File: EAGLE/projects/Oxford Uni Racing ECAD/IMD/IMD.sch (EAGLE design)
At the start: 6 parts, among them IC1 LM2901N, J1 T821108A1S100CEU, K1 RT444012, T1 BT169

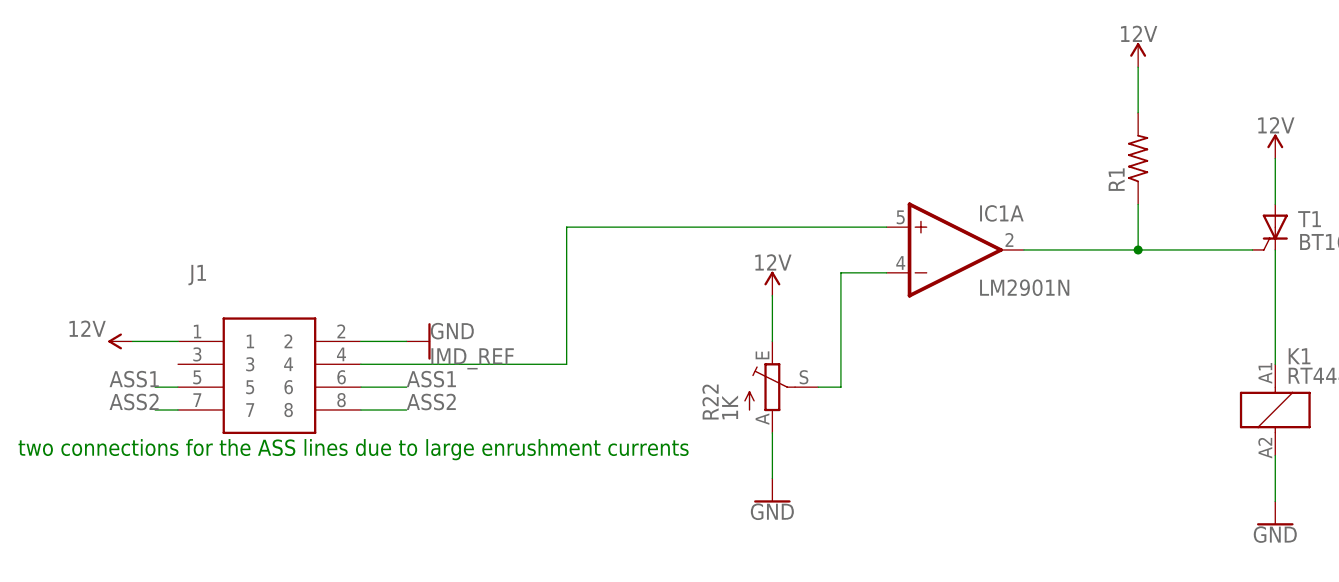
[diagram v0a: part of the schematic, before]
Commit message: routed IMD
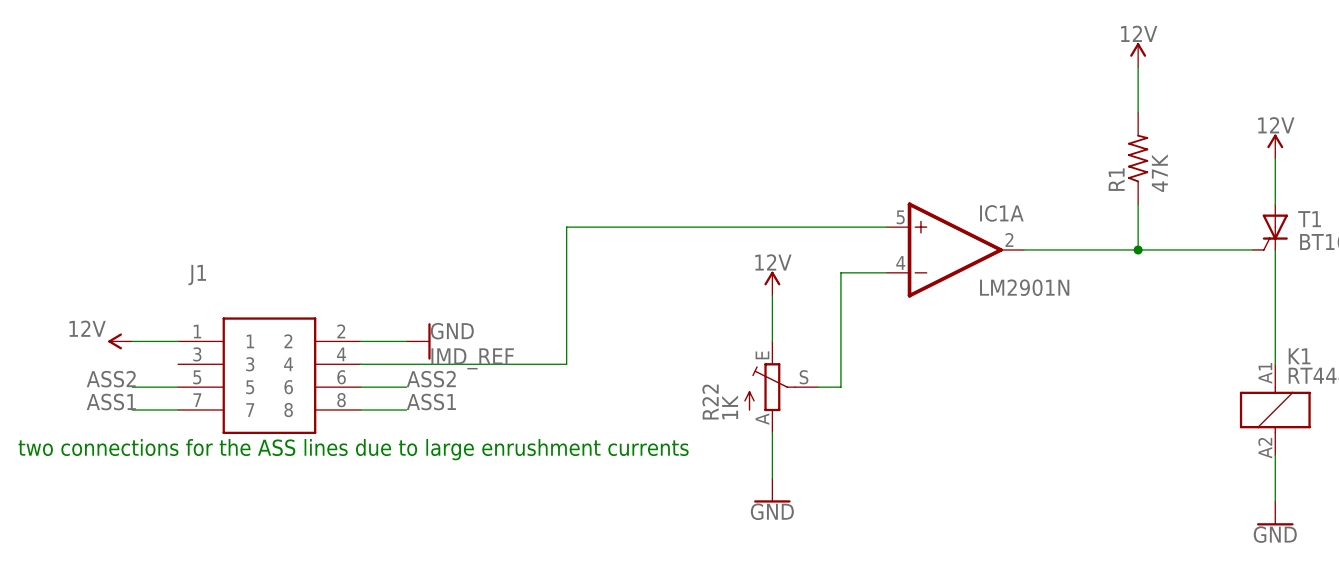
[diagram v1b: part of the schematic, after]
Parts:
- R1: value (none) -> 47K
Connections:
- net ASS1: now also J1.7, J1.8; no longer J1.5, J1.6
- net ASS2: now also J1.5, J1.6; no longer J1.7, J1.8
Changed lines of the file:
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@@
 <part name="GND3" library="SparkFun-PowerSymbols" library_urn="urn:adsk.eagle:library:530" deviceset="GND" device=""/>
 <part name="GND4" library="SparkFun-PowerSymbols" library_urn="urn:adsk.eagle:library:530" deviceset="GND" device=""/>
-<part name="R1" library="adafruit" library_urn="urn:adsk.eagle:library:420" deviceset="R-US_" device="0204/7" package3d_urn="urn:adsk.eagle:package:6240596/1"/>
+<part name="R1" library="adafruit" library_urn="urn:adsk.eagle:library:420" deviceset="R-US_" device="0204/7" package3d_urn="urn:adsk.eagle:package:6240596/1" value="47K"/>
 <part name="SUPPLY4" library="SparkFun-PowerSymbols" library_urn="urn:adsk.eagle:library:530" deviceset="12V" device=""/>
 </parts>
@@
 </segment>
 <segment>
-<pinref part="J1" gate="G$1" pin="6"/>
-<wire x1="58.42" y1="22.86" x2="63.5" y2="22.86" width="0.1524" layer="91"/>
-<label x="63.5" y="22.86" size="1.778" layer="95"/>
-</segment>
-<segment>
-<pinref part="J1" gate="G$1" pin="5"/>
-<wire x1="38.1" y1="22.86" x2="35.56" y2="22.86" width="0.1524" layer="91"/>
-<label x="30.48" y="22.86" size="1.778" layer="95"/>
+<pinref part="J1" gate="G$1" pin="7"/>
+<wire x1="38.1" y1="20.32" x2="33.02" y2="20.32" width="0.1524" layer="91"/>
+<label x="27.94" y="20.32" size="1.778" layer="95"/>
+</segment>
+<segment>
+<pinref part="J1" gate="G$1" pin="8"/>
+<wire x1="63.5" y1="20.32" x2="58.42" y2="20.32" width="0.1524" layer="91"/>
+<label x="63.5" y="20.32" size="1.778" layer="95"/>
 </segment>
 </net>
 <net name="ASS2" class="0">
-<segment>
-<pinref part="J1" gate="G$1" pin="8"/>
-<wire x1="58.42" y1="20.32" x2="63.5" y2="20.32" width="0.1524" layer="91"/>
-<label x="63.5" y="20.32" size="1.778" layer="95"/>
-</segment>
 <segment>
 <pinref part="K1" gate="2" pin="P"/>
@@
 </segment>
 <segment>
-<pinref part="J1" gate="G$1" pin="7"/>
-<wire x1="38.1" y1="20.32" x2="35.56" y2="20.32" width="0.1524" layer="91"/>
-<label x="30.48" y="20.32" size="1.778" layer="95"/>
-</segment>
-</net>
+<pinref part="J1" gate="G$1" pin="6"/>
+<wire x1="58.42" y1="22.86" x2="63.5" y2="22.86" width="0.1524" layer="91"/>
+<label x="63.5" y="22.86" size="1.778" layer="95"/>
+</segment>
+<segment>
+<pinref part="J1" gate="G$1" pin="5"/>
+<wire x1="38.1" y1="22.86" x2="33.02" y2="22.86" width="0.1524" layer="91"/>
+<label x="27.94" y="22.86" size="1.778" layer="95"/>
+</segment>
+</net>

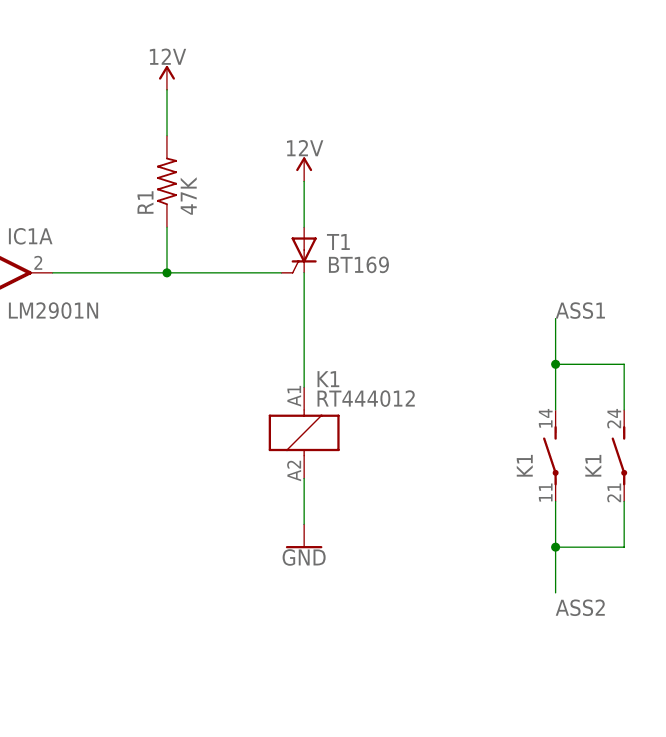
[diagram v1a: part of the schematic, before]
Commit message: fixed IMD with a MOSFET rather than a thyristor
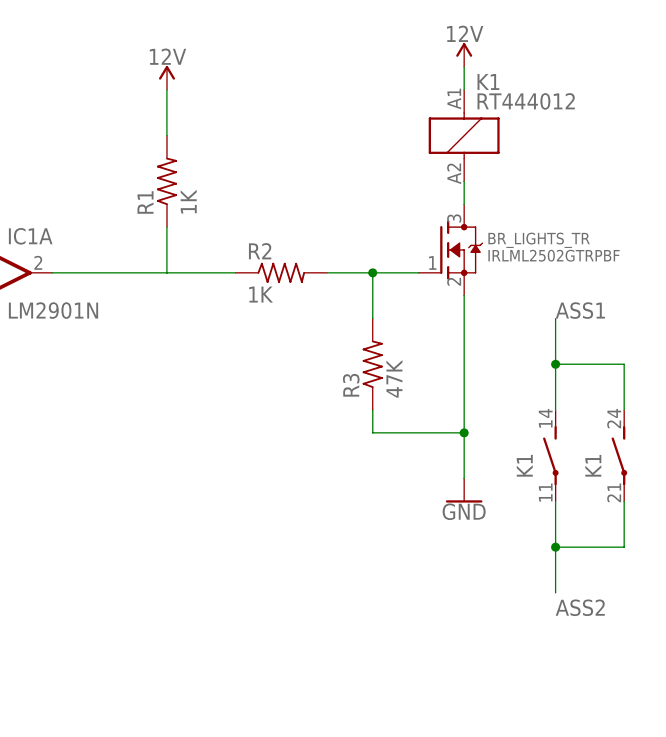
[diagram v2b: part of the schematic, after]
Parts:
- removed T1: BT169, triac:BT169
- added BR_LIGHTS_TR: IRLML2502GTRPBF, adafruit:MOSFET-NREFLOW
- added R2: 1K, adafruit:R-US_0204/7
- added R3: 47K, adafruit:R-US_0204/7
- R1: value 47K -> 1K
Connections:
- new net N$6: BR_LIGHTS_TR.D, K11.2
- net 12V: now also K11.1; no longer T1.A
- net GND: now also BR_LIGHTS_TR.S, R3.1; no longer K11.2
- net N$1: now also R2.1; no longer T1.G
- net N$3: now also BR_LIGHTS_TR.G, R2.2, R3.2; no longer K11.1, T1.C
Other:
- moved on the sheet: K1
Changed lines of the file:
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@@
 <part name="R22" library="pot" library_urn="urn:adsk.eagle:library:331" deviceset="TRIM_EU-" device="B90P" package3d_urn="urn:adsk.eagle:package:22714/1" value="1K"/>
 <part name="IC1" library="linear" library_urn="urn:adsk.eagle:library:262" deviceset="LM2901" device="N" package3d_urn="urn:adsk.eagle:package:16407/2"/>
-<part name="T1" library="triac" library_urn="urn:adsk.eagle:library:403" deviceset="BT169" device="" package3d_urn="urn:adsk.eagle:package:30142/1"/>
 <part name="K1" library="relay" library_urn="urn:adsk.eagle:library:339" deviceset="RT44?*" device="4" package3d_urn="urn:adsk.eagle:package:24520/1" technology="012"/>
 <part name="SUPPLY1" library="SparkFun-PowerSymbols" library_urn="urn:adsk.eagle:library:530" deviceset="12V" device=""/>
@@
 <part name="GND1" library="SparkFun-PowerSymbols" library_urn="urn:adsk.eagle:library:530" deviceset="GND" device=""/>
 <part name="GND2" library="SparkFun-PowerSymbols" library_urn="urn:adsk.eagle:library:530" deviceset="GND" device=""/>
-<part name="GND3" library="SparkFun-PowerSymbols" library_urn="urn:adsk.eagle:library:530" deviceset="GND" device=""/>
 <part name="GND4" library="SparkFun-PowerSymbols" library_urn="urn:adsk.eagle:library:530" deviceset="GND" device=""/>
-<part name="R1" library="adafruit" library_urn="urn:adsk.eagle:library:420" deviceset="R-US_" device="0204/7" package3d_urn="urn:adsk.eagle:package:6240596/1" value="47K"/>
+<part name="R1" library="adafruit" library_urn="urn:adsk.eagle:library:420" deviceset="R-US_" device="0204/7" package3d_urn="urn:adsk.eagle:package:6240596/1" value="1K"/>
 <part name="SUPPLY4" library="SparkFun-PowerSymbols" library_urn="urn:adsk.eagle:library:530" deviceset="12V" device=""/>
+<part name="BR_LIGHTS_TR" library="adafruit" library_urn="urn:adsk.eagle:library:420" deviceset="MOSFET-N" device="REFLOW" package3d_urn="urn:adsk.eagle:package:6240836/1" value="IRLML2502GTRPBF"/>
+<part name="R2" library="adafruit" library_urn="urn:adsk.eagle:library:420" deviceset="R-US_" device="0204/7" package3d_urn="urn:adsk.eagle:package:6240596/1" value="1K"/>
+<part name="R3" library="adafruit" library_urn="urn:adsk.eagle:library:420" deviceset="R-US_" device="0204/7" package3d_urn="urn:adsk.eagle:package:6240596/1" value="47K"/>
+<part name="GND20" library="SparkFun-PowerSymbols" library_urn="urn:adsk.eagle:library:530" deviceset="GND" device=""/>
 </parts>
 <sheets>
@@
 <attribute name="VALUE" x="81.28" y="-68.58" size="1.778" layer="96"/>
 </instance>
-<instance part="T1" gate="1" x="160.02" y="40.64" smashed="yes">
-<attribute name="NAME" x="162.56" y="40.64" size="1.778" layer="95"/>
-<attribute name="VALUE" x="162.56" y="38.1" size="1.778" layer="96"/>
-</instance>
-<instance part="K1" gate="1" x="160.02" y="20.32" smashed="yes">
-<attribute name="VALUE" x="161.29" y="23.241" size="1.778" layer="96"/>
-<attribute name="PART" x="161.29" y="25.4" size="1.778" layer="95"/>
+<instance part="K1" gate="1" x="177.8" y="53.34" smashed="yes">
+<attribute name="VALUE" x="179.07" y="56.261" size="1.778" layer="96"/>
+<attribute name="PART" x="179.07" y="58.42" size="1.778" layer="95"/>
 </instance>
 <instance part="K1" gate="2" x="187.96" y="17.78" smashed="yes">
@@
 <attribute name="VALUE" x="27.94" y="30.226" size="1.778" layer="96" rot="R180" align="bottom-center"/>
 </instance>
-<instance part="SUPPLY2" gate="G$1" x="160.02" y="48.26" smashed="yes">
-<attribute name="VALUE" x="160.02" y="51.054" size="1.778" layer="96" align="bottom-center"/>
+<instance part="SUPPLY2" gate="G$1" x="177.8" y="60.96" smashed="yes">
+<attribute name="VALUE" x="177.8" y="63.754" size="1.778" layer="96" align="bottom-center"/>
 </instance>
 <instance part="SUPPLY3" gate="G$1" x="144.78" y="58.42" smashed="yes">
@@
 <instance part="GND2" gate="1" x="104.14" y="10.16" smashed="yes">
 <attribute name="VALUE" x="104.14" y="9.906" size="1.778" layer="96" align="top-center"/>
-</instance>
-<instance part="GND3" gate="1" x="160.02" y="7.62" smashed="yes">
-<attribute name="VALUE" x="160.02" y="7.366" size="1.778" layer="96" align="top-center"/>
 </instance>
 <instance part="GND4" gate="1" x="50.8" y="-45.72" smashed="yes" rot="R270">
@@
 <instance part="SUPPLY4" gate="G$1" x="104.14" y="33.02" smashed="yes">
 <attribute name="VALUE" x="104.14" y="35.814" size="1.778" layer="96" align="bottom-center"/>
+</instance>
+<instance part="BR_LIGHTS_TR" gate="G$1" x="175.26" y="40.64" smashed="yes">
+<attribute name="NAME" x="180.34" y="41.275" size="1.27" layer="95"/>
+<attribute name="VALUE" x="180.34" y="39.37" size="1.27" layer="96"/>
+</instance>
+<instance part="R2" gate="G$1" x="157.48" y="38.1" smashed="yes">
+<attribute name="NAME" x="153.67" y="39.5986" size="1.778" layer="95"/>
+<attribute name="VALUE" x="153.67" y="34.798" size="1.778" layer="96"/>
+</instance>
+<instance part="R3" gate="G$1" x="167.64" y="27.94" smashed="yes" rot="R90">
+<attribute name="NAME" x="166.1414" y="24.13" size="1.778" layer="95" rot="R90"/>
+<attribute name="VALUE" x="170.942" y="24.13" size="1.778" layer="96" rot="R90"/>
+</instance>
+<instance part="GND20" gate="1" x="177.8" y="12.7" smashed="yes">
+<attribute name="VALUE" x="177.8" y="12.446" size="1.778" layer="96" align="top-center"/>
 </instance>
 </instances>
@@
 </segment>
 <segment>
-<pinref part="K1" gate="1" pin="2"/>
-<pinref part="GND3" gate="1" pin="GND"/>
-<wire x1="160.02" y1="15.24" x2="160.02" y2="10.16" width="0.1524" layer="91"/>
-</segment>
-<segment>
 <pinref part="J1" gate="G$1" pin="2"/>
 <pinref part="GND1" gate="1" pin="GND"/>
@@
 <wire x1="104.14" y1="17.78" x2="104.14" y2="12.7" width="0.1524" layer="91"/>
 </segment>
+<segment>
+<pinref part="BR_LIGHTS_TR" gate="G$1" pin="S"/>
+<pinref part="GND20" gate="1" pin="GND"/>
+<wire x1="177.8" y1="35.56" x2="177.8" y2="20.32" width="0.1524" layer="91"/>
+<pinref part="R3" gate="G$1" pin="1"/>
+<wire x1="177.8" y1="20.32" x2="177.8" y2="15.24" width="0.1524" layer="91"/>
+<wire x1="167.64" y1="22.86" x2="167.64" y2="20.32" width="0.1524" layer="91"/>
+<wire x1="167.64" y1="20.32" x2="177.8" y2="20.32" width="0.1524" layer="91"/>
+<junction x="177.8" y="20.32"/>
+</segment>
 </net>
 <net name="N$1" class="0">
 <segment>
 <pinref part="IC1" gate="A" pin="OUT"/>
-<pinref part="T1" gate="1" pin="G"/>
 <wire x1="132.08" y1="38.1" x2="144.78" y2="38.1" width="0.1524" layer="91"/>
 <pinref part="R1" gate="G$1" pin="1"/>
-<wire x1="144.78" y1="38.1" x2="157.48" y2="38.1" width="0.1524" layer="91"/>
 <wire x1="144.78" y1="38.1" x2="144.78" y2="43.18" width="0.1524" layer="91"/>
-<junction x="144.78" y="38.1"/>
+<pinref part="R2" gate="G$1" pin="1"/>
+<wire x1="144.78" y1="38.1" x2="152.4" y2="38.1" width="0.1524" layer="91"/>
 </segment>
 </net>
@@
 <segment>
 <pinref part="SUPPLY2" gate="G$1" pin="12V"/>
-<pinref part="T1" gate="1" pin="A"/>
-<wire x1="160.02" y1="48.26" x2="160.02" y2="43.18" width="0.1524" layer="91"/>
+<wire x1="177.8" y1="60.96" x2="177.8" y2="58.42" width="0.1524" layer="91"/>
+<pinref part="K1" gate="1" pin="1"/>
 </segment>
 <segment>
@@
 <pinref part="R22" gate="1" pin="E"/>
 <wire x1="104.14" y1="33.02" x2="104.14" y2="27.94" width="0.1524" layer="91"/>
-</segment>
-</net>
-<net name="N$3" class="0">
-<segment>
-<pinref part="T1" gate="1" pin="C"/>
-<pinref part="K1" gate="1" pin="1"/>
-<wire x1="160.02" y1="38.1" x2="160.02" y2="25.4" width="0.1524" layer="91"/>
 </segment>
 </net>
@@
 </segment>
 </net>
+<net name="N$3" class="0">
+<segment>
+<pinref part="R2" gate="G$1" pin="2"/>
+<pinref part="BR_LIGHTS_TR" gate="G$1" pin="G"/>
+<wire x1="162.56" y1="38.1" x2="167.64" y2="38.1" width="0.1524" layer="91"/>
+<pinref part="R3" gate="G$1" pin="2"/>
+<wire x1="167.64" y1="38.1" x2="172.72" y2="38.1" width="0.1524" layer="91"/>
+<wire x1="167.64" y1="38.1" x2="167.64" y2="33.02" width="0.1524" layer="91"/>
+<junction x="167.64" y="38.1"/>
+</segment>
+</net>
+<net name="N$6" class="0">
+<segment>
+<pinref part="BR_LIGHTS_TR" gate="G$1" pin="D"/>
+<wire x1="177.8" y1="48.26" x2="177.8" y2="45.72" width="0.1524" layer="91"/>
+<pinref part="K1" gate="1" pin="2"/>
+</segment>
+</net>

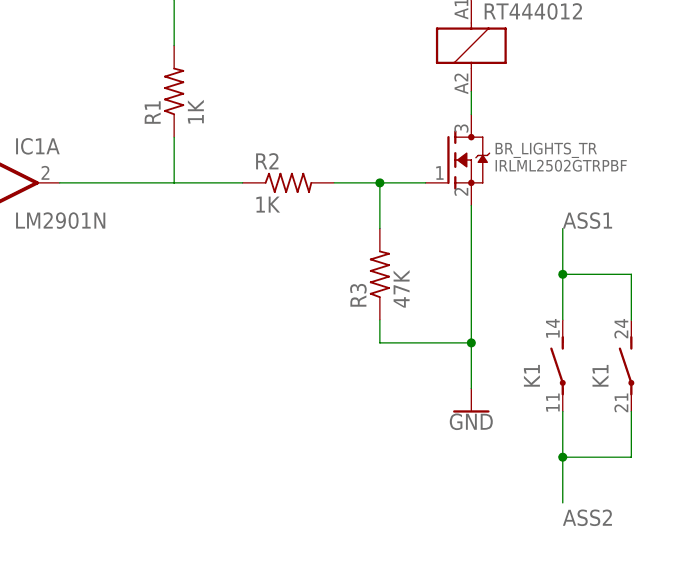
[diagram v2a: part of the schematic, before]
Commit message: removed unnecessary pulldown resistors
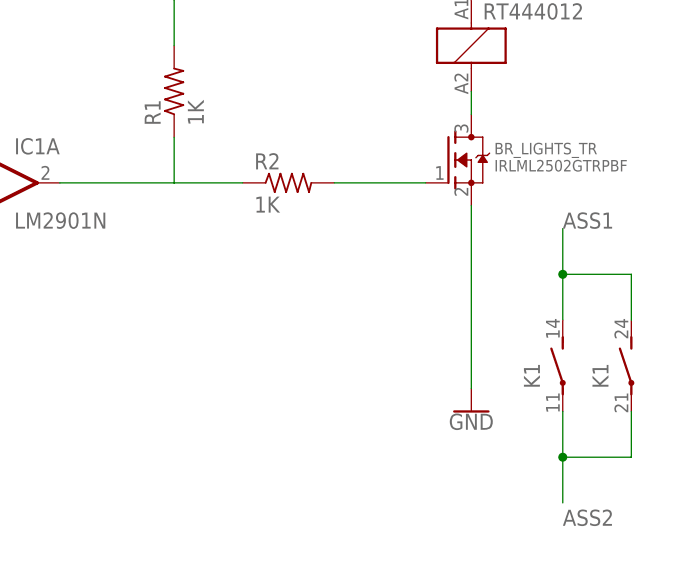
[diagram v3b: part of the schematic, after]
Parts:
- removed R3: 47K, adafruit:R-US_0204/7
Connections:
- net GND: no longer R3.1
- net N$3: no longer R3.2
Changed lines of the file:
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@@
 <part name="BR_LIGHTS_TR" library="adafruit" library_urn="urn:adsk.eagle:library:420" deviceset="MOSFET-N" device="REFLOW" package3d_urn="urn:adsk.eagle:package:6240836/1" value="IRLML2502GTRPBF"/>
 <part name="R2" library="adafruit" library_urn="urn:adsk.eagle:library:420" deviceset="R-US_" device="0204/7" package3d_urn="urn:adsk.eagle:package:6240596/1" value="1K"/>
-<part name="R3" library="adafruit" library_urn="urn:adsk.eagle:library:420" deviceset="R-US_" device="0204/7" package3d_urn="urn:adsk.eagle:package:6240596/1" value="47K"/>
 <part name="GND20" library="SparkFun-PowerSymbols" library_urn="urn:adsk.eagle:library:530" deviceset="GND" device=""/>
 </parts>
@@
 <attribute name="NAME" x="153.67" y="39.5986" size="1.778" layer="95"/>
 <attribute name="VALUE" x="153.67" y="34.798" size="1.778" layer="96"/>
-</instance>
-<instance part="R3" gate="G$1" x="167.64" y="27.94" smashed="yes" rot="R90">
-<attribute name="NAME" x="166.1414" y="24.13" size="1.778" layer="95" rot="R90"/>
-<attribute name="VALUE" x="170.942" y="24.13" size="1.778" layer="96" rot="R90"/>
 </instance>
 <instance part="GND20" gate="1" x="177.8" y="12.7" smashed="yes">
@@
 <pinref part="BR_LIGHTS_TR" gate="G$1" pin="S"/>
 <pinref part="GND20" gate="1" pin="GND"/>
-<wire x1="177.8" y1="35.56" x2="177.8" y2="20.32" width="0.1524" layer="91"/>
-<pinref part="R3" gate="G$1" pin="1"/>
-<wire x1="177.8" y1="20.32" x2="177.8" y2="15.24" width="0.1524" layer="91"/>
-<wire x1="167.64" y1="22.86" x2="167.64" y2="20.32" width="0.1524" layer="91"/>
-<wire x1="167.64" y1="20.32" x2="177.8" y2="20.32" width="0.1524" layer="91"/>
-<junction x="177.8" y="20.32"/>
+<wire x1="177.8" y1="35.56" x2="177.8" y2="15.24" width="0.1524" layer="91"/>
 </segment>
 </net>
@@
 <pinref part="R2" gate="G$1" pin="2"/>
 <pinref part="BR_LIGHTS_TR" gate="G$1" pin="G"/>
-<wire x1="162.56" y1="38.1" x2="167.64" y2="38.1" width="0.1524" layer="91"/>
-<pinref part="R3" gate="G$1" pin="2"/>
-<wire x1="167.64" y1="38.1" x2="172.72" y2="38.1" width="0.1524" layer="91"/>
-<wire x1="167.64" y1="38.1" x2="167.64" y2="33.02" width="0.1524" layer="91"/>
-<junction x="167.64" y="38.1"/>
-</segment>
-</net>
+<wire x1="162.56" y1="38.1" x2="172.72" y2="38.1" width="0.1524" layer="91"/>
+</segment>
+</net>
